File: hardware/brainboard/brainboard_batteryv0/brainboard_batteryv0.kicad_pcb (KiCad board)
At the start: 2 copper layers, 86.4 x 54.6 mm, 64 parts, among them CON1 USB-MINI-B, P1 JST, P10 3V3, P2 VBAT, P3 GND, P4 BBB_PMIC, P5 ~ALRT, P6 VBUS, P7 WP, P8 EN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

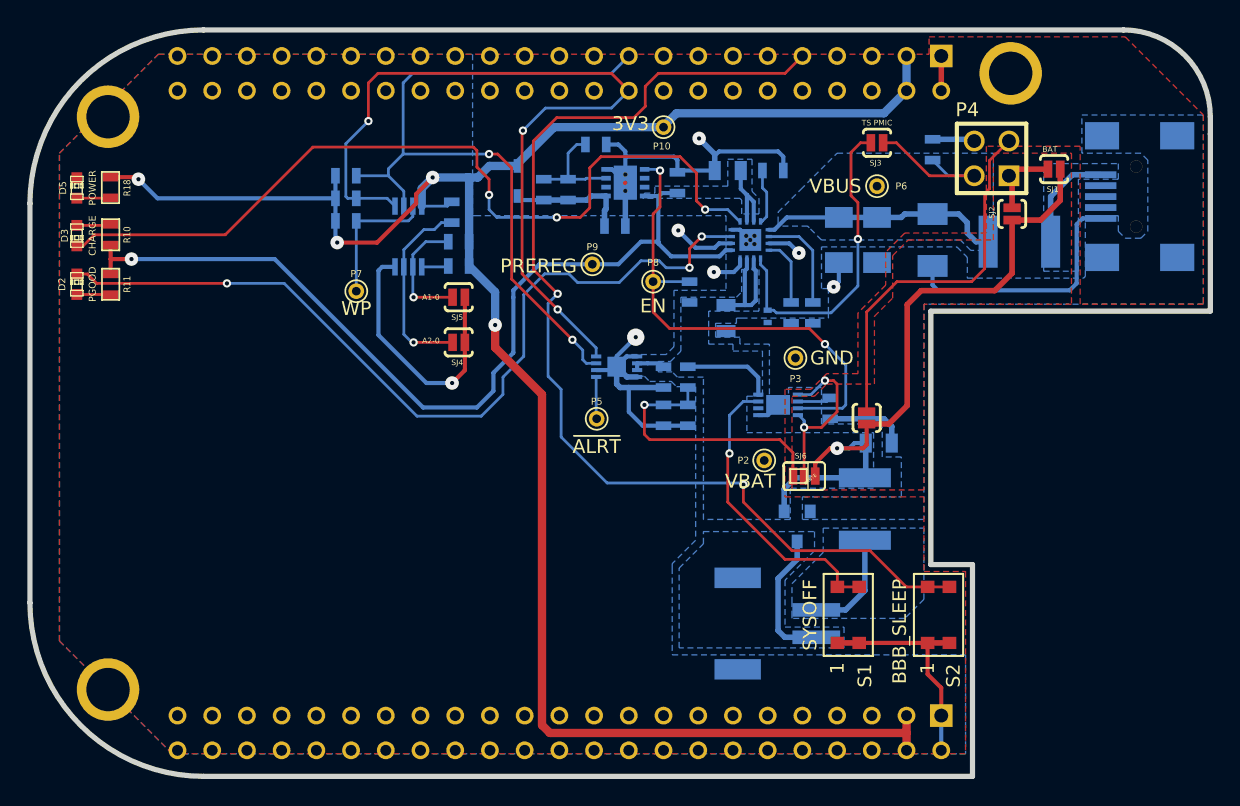
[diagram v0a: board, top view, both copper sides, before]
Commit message: Thesis version
Finally able to commit again (Windows XP issues fixed by OS upgrade).
Added latest version of wearable BB, along with prototype "muscleboard"
2-channel board for EMG/ECG applications
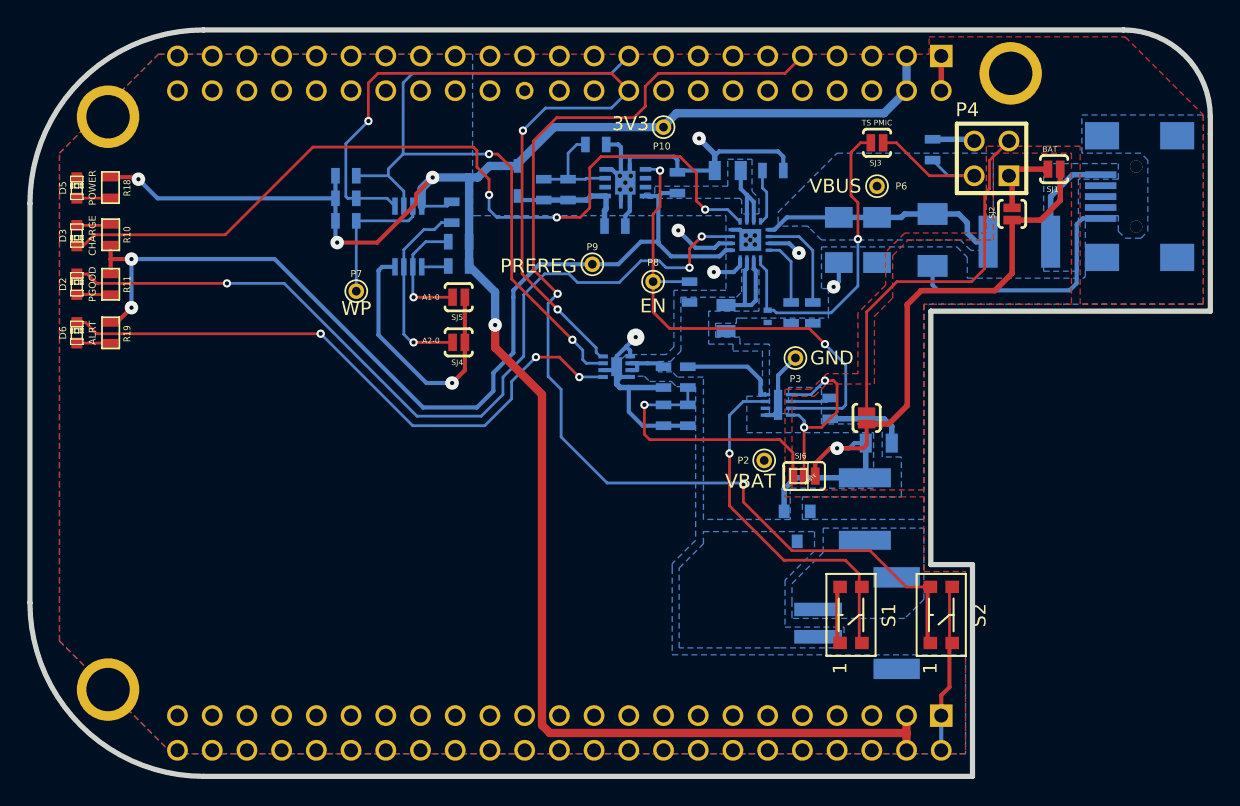
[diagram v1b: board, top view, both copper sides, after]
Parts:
- removed P5: ~ALRT, PINTST
- added D6: ALRT, LED-0603, F.Cu at (186.6, 131.8)
- added R19: 2.2k, SM0603, F.Cu at (189.0, 131.8)
- U1: footprint tdfn8 -> tdfn8-2x2
- U4: footprint hvson8-vias -> s-pvson-n8-vias
- U5: footprint dfn8-2x3 -> dfn8-3x2
- moved P1 0.14 mm to (240.8, 153.0), turned to 270 degrees
- turned U1 to 180 degrees
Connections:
- P1 pad 1: /B- -> /B+
- P1 pad 2: /B+ -> /B-
- S2 pad 1: GND -> /PWR_BUT
- S2 pad 2: /PWR_BUT -> GND
- S2 pad 3: GND -> /PWR_BUT
- S2 pad 4: /PWR_BUT -> GND
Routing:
- net /~ALRT: track 3.08 -> 45.1 mm, vias 0 -> 3
- net /B-: track 10.1 -> 0.00 mm
- net /B+: track 7.82 -> 0.00 mm
- net /OUT: track 73.1 -> 78.6 mm, vias 1 -> 2
- net GND: track 126.6 -> 132.0 mm
- net /~PB: track 21.8 -> 26.3 mm
- net /PWR_BUT: track 80.1 -> 82.6 mm
- net N-0000020: track 0.00 -> 2.48 mm
- net +BATT: track 67.9 -> 69.4 mm
- net /~KILL: track 13.1 -> 14.2 mm
- net /EN: track 36.6 -> 37.2 mm
- net /OFFT: track 2.47 -> 2.99 mm
- net /SCL: track 55.2 -> 55.7 mm
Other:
- net class High Current: via_dia 0.31 -> 0.9906; via_drill 0.3 -> 0.8128
